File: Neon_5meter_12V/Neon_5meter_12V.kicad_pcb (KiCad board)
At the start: 2 copper layers, 46 parts, among them J1 Conn_01x16_Pin, J2 Barrel_Jack_MountingPin, J3 Conn_01x16_Pin, J4 Barrel_Jack_MountingPin, J5 Barrel_Jack_MountingPin, J6 Conn_01x03_Pin, Q1 IRLML2502TRPBF, Q2 IRLML2502TRPBF, Q3 BSS138, Q4 BSS138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

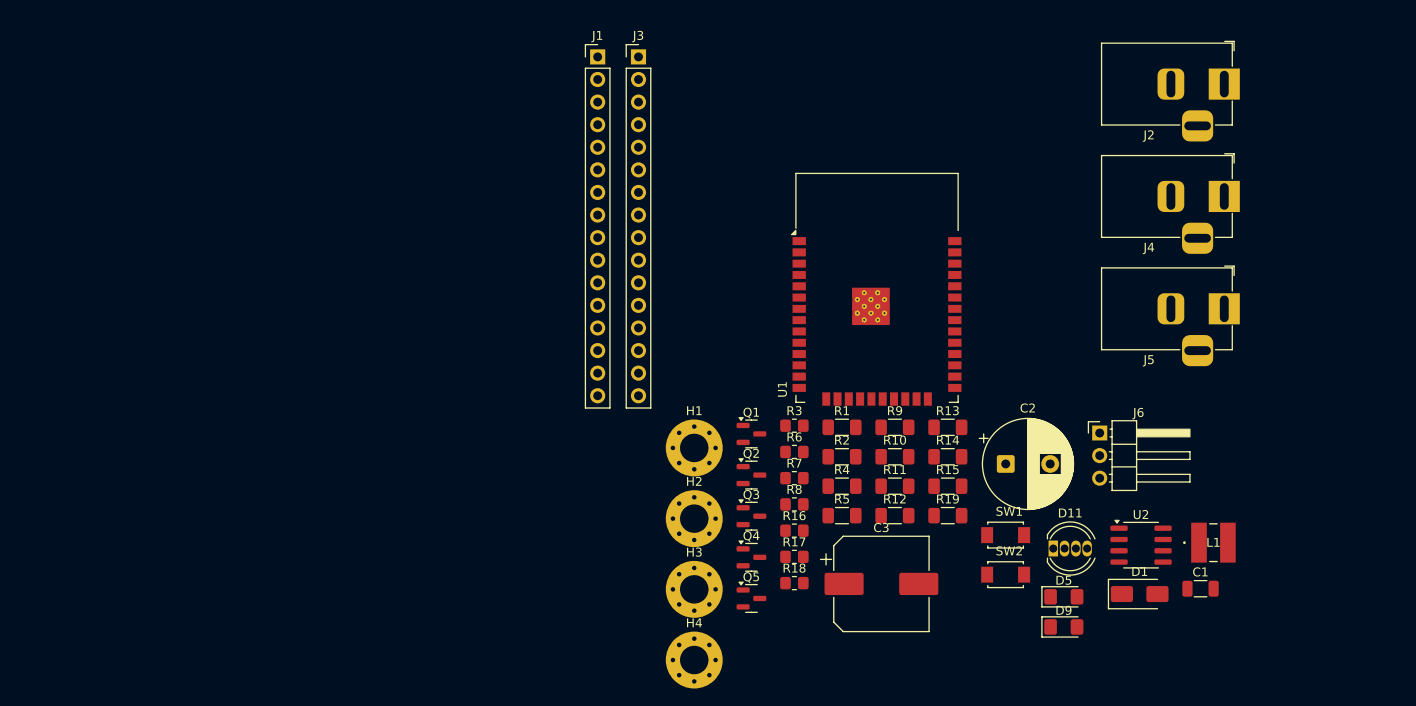
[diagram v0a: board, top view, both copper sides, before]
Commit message: updated esp32 footprint keepout zone
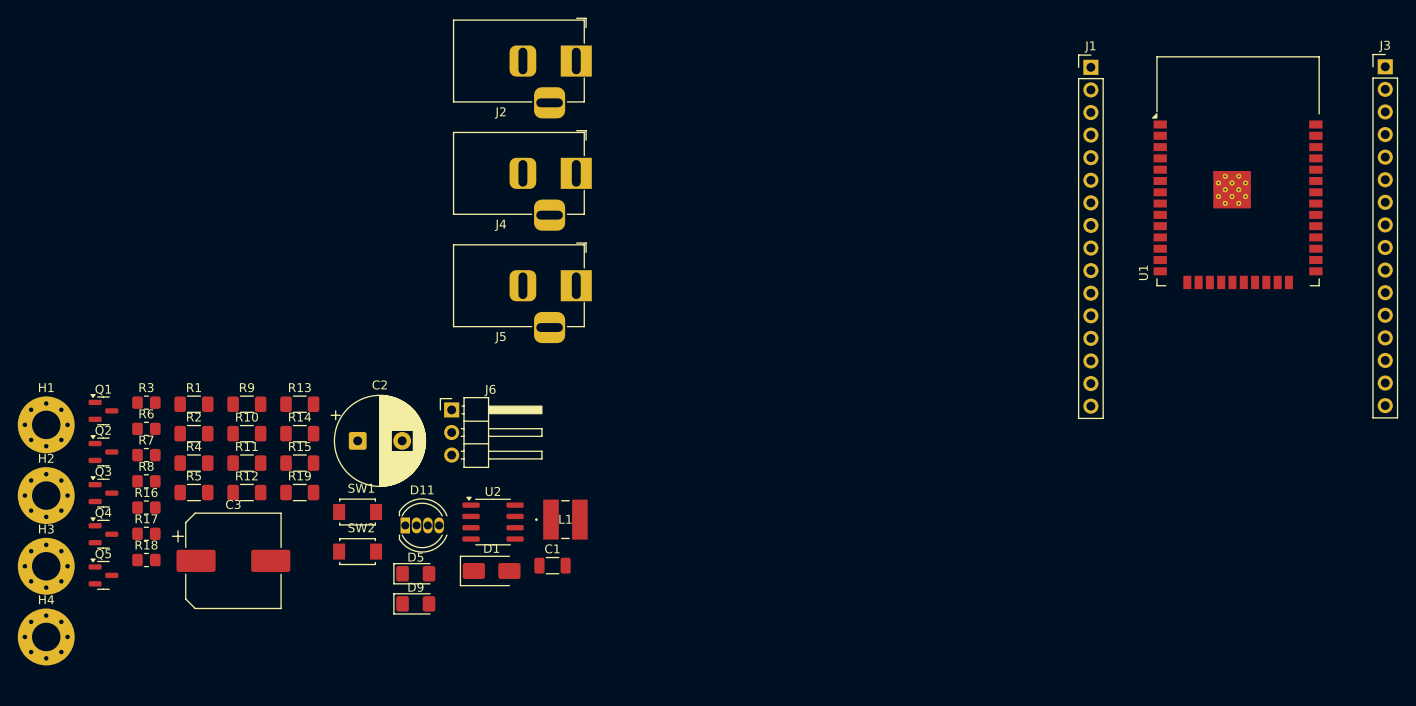
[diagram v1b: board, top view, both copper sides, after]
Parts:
- moved J3 84.0 mm to (179.9, 36.9)
- moved C2 72.9 mm to (64.4, 79.0)
- moved C3 72.9 mm to (50.4, 92.5)
- moved H1 72.9 mm to (29.3, 77.2)
- moved H2 72.9 mm to (29.3, 85.1)
- moved H3 72.9 mm to (29.3, 93.1)
- moved H4 72.9 mm to (29.3, 101.0)
- moved J2 72.9 mm to (88.9, 36.2)
- moved J4 72.9 mm to (88.9, 48.9)
- moved J5 72.9 mm to (88.9, 61.5)
- moved R1 72.9 mm to (45.9, 74.8)
- moved R10 72.9 mm to (51.9, 78.2)
- moved R11 72.9 mm to (51.9, 81.5)
- moved R12 72.9 mm to (51.9, 84.8)
- moved R13 72.9 mm to (57.8, 74.8)
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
